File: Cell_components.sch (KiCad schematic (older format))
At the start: 12 parts, among them Q6 Q_NMOS_GSD

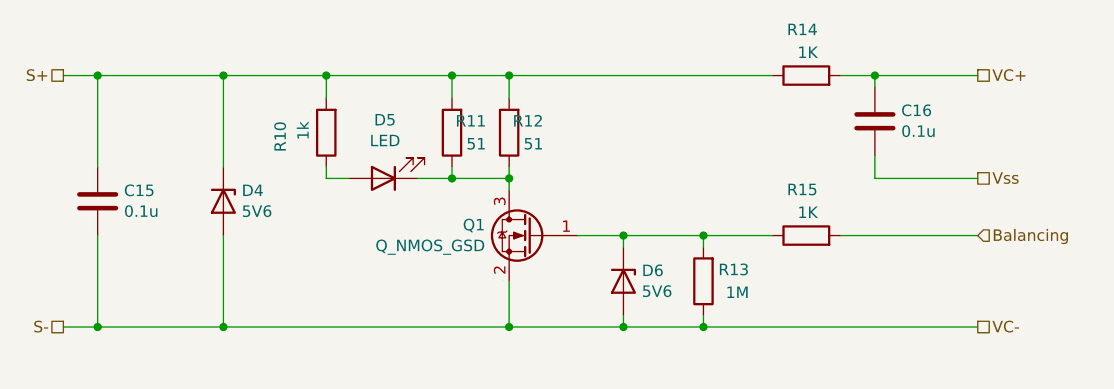
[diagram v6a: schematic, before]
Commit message: Add files via upload
Placed additional via's to BQ76-IC and removed soldermask beneath (to allow for soldering of thermal pad without hot air). Generated GERBER-, BOM- (for SMD parts) and POS-file.
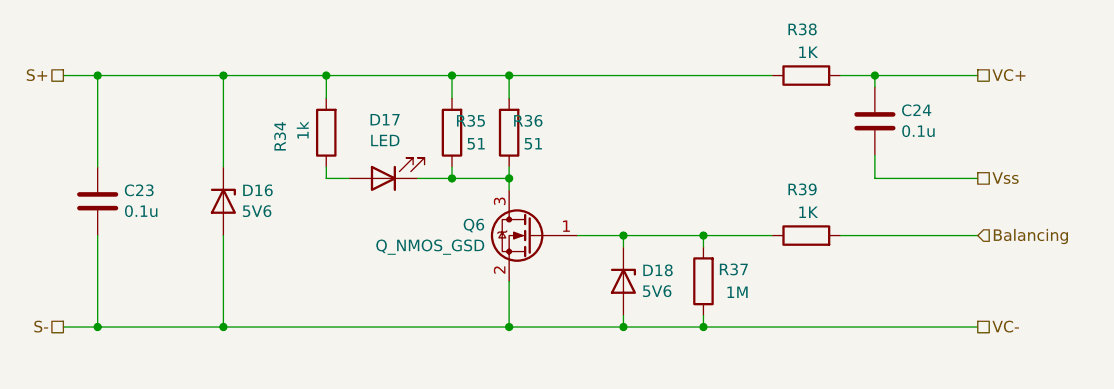
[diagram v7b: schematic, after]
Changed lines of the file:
@@
 $Descr User 7874 5906
 encoding utf-8
-Sheet 3 7
+Sheet 7 7
 Title ""
 Date ""
@@
 AR Path="/5FA9BBC5/5FB16918" Ref="C19"  Part="1"
 AR Path="/5FA9D4E1/5FB16918" Ref="C21"  Part="1"
-F 0 "C15" H 1965 2096 50  0000 L CNN
+F 0 "C23" H 1965 2096 50  0000 L CNN
 F 1 "0.1u " H 1965 2005 50  0000 L CNN
 F 2 "Capacitor_SMD:C_0805_2012Metric_Pad1.15x1.40mm_HandSolder" H 1888 1900 50  0001 C CNN
@@
 AR Path="/5FA9BBC5/5FB1FCF3" Ref="C20"  Part="1"
 AR Path="/5FA9D4E1/5FB1FCF3" Ref="C22"  Part="1"
-F 0 "C16" H 5365 1746 50  0000 L CNN
+F 0 "C24" H 5365 1746 50  0000 L CNN
 F 1 "0.1u " H 5365 1655 50  0000 L CNN
 F 2 "Capacitor_SMD:C_0805_2012Metric_Pad1.15x1.40mm_HandSolder" H 5288 1550 50  0001 C CNN
@@
 AR Path="/5FA9D4E1/5FB211C7" Ref="R32"  Part="1"
 AR Path="/5FAA7870/5FB211C7" Ref="R38"  Part="1"
-F 0 "R14" V 5150 1450 50  0000 L CNN
+F 0 "R38" V 5150 1450 50  0000 L CNN
 F 1 "1K" V 5050 1450 50  0000 L CNN
 F 2 "Resistor_SMD:R_0603_1608Metric_Pad1.05x0.95mm_HandSolder" V 4880 1500 50  0001 C CNN
@@
 AR Path="/5FA9D4E1/5FB24803" Ref="R33"  Part="1"
 AR Path="/5FAA7870/5FB24803" Ref="R39"  Part="1"
-F 0 "R15" V 5150 2150 50  0000 L CNN
+F 0 "R39" V 5150 2150 50  0000 L CNN
 F 1 "1K" V 5050 2150 50  0000 L CNN
 F 2 "Resistor_SMD:R_0603_1608Metric_Pad1.05x0.95mm_HandSolder" V 4880 2200 50  0001 C CNN
@@
 AR Path="/5FA9D4E1/5FB273BA" Ref="R31"  Part="1"
 AR Path="/5FAA7870/5FB273BA" Ref="R37"  Part="1"
-F 0 "R13" H 4300 2350 50  0000 L CNN
+F 0 "R37" H 4300 2350 50  0000 L CNN
 F 1 "1M" H 4300 2450 50  0000 L CNN
 F 2 "Resistor_SMD:R_0805_2012Metric_Pad1.15x1.40mm_HandSolder" V 4430 2400 50  0001 C CNN
@@
 AR Path="/5FA9BBC5/5FB35DA2" Ref="D12"  Part="1"
 AR Path="/5FA9D4E1/5FB35DA2" Ref="D15"  Part="1"
-F 0 "D6" V 4104 2480 50  0000 L CNN
+F 0 "D18" V 4104 2480 50  0000 L CNN
 F 1 "5V6" V 4195 2480 50  0000 L CNN
 F 2 "Diode_SMD:D_SOD-123" H 4150 2400 50  0001 C CNN
@@
 AR Path="/5FA9D4E1/5FAFC2A5" Ref="R30"  Part="1"
 AR Path="/5FAA7870/5FAFC2A5" Ref="R36"  Part="1"
-F 0 "R12" H 3500 1700 50  0000 L CNN
+F 0 "R36" H 3500 1700 50  0000 L CNN
 F 1 "51" H 3500 1800 50  0000 L CNN
 F 2 "Resistor_SMD:R_2512_6332Metric_Pad1.52x3.35mm_HandSolder" V 3580 1750 50  0001 C CNN
@@
 AR Path="/5FA9D4E1/5FAFE41B" Ref="R29"  Part="1"
 AR Path="/5FAA7870/5FAFE41B" Ref="R35"  Part="1"
-F 0 "R11" H 3250 1700 50  0000 L CNN
+F 0 "R35" H 3250 1700 50  0000 L CNN
 F 1 "51" H 3250 1800 50  0000 L CNN
 F 2 "Resistor_SMD:R_2512_6332Metric_Pad1.52x3.35mm_HandSolder" V 3330 1750 50  0001 C CNN
@@
 AR Path="/5FA9D4E1/5FB07EF1" Ref="R28"  Part="1"
 AR Path="/5FAA7870/5FB07EF1" Ref="R34"  Part="1"
-F 0 "R10" V 3050 1700 50  0000 L CNN
+F 0 "R34" V 3050 1700 50  0000 L CNN
 F 1 "1k" V 2950 1700 50  0000 L CNN
 F 2 "Resistor_SMD:R_0603_1608Metric_Pad1.05x0.95mm_HandSolder" V 2780 1750 50  0001 C CNN
@@
 AR Path="/5FA9D4E1/5FB0934F" Ref="D14"  Part="1"
 AR Path="/5FAA7870/5FB0934F" Ref="D17"  Part="1"
-F 0 "D5" H 3093 1695 50  0000 C CNN
+F 0 "D17" H 3093 1695 50  0000 C CNN
 F 1 "LED" H 3093 1786 50  0000 C CNN
 F 2 "LED_SMD:LED_0805_2012Metric_Pad1.15x1.40mm_HandSolder" H 3100 1950 50  0001 C CNN
@@
 AR Path="/5FA9BBC5/601F5F7C" Ref="Q4"  Part="1"
 AR Path="/5FA9D4E1/601F5F7C" Ref="Q5"  Part="1"
-F 0 "Q1" H 3955 2246 50  0000 L CNN
+F 0 "Q6" H 3955 2246 50  0000 L CNN
 F 1 "Q_NMOS_GSD" H 3955 2155 50  0000 L CNN
 F 2 "Package_TO_SOT_SMD:SOT-23" H 3950 2300 50  0001 C CNN
@@
 AR Path="/5FA9BBC5/5FB3410E" Ref="D10"  Part="1"
 AR Path="/5FA9D4E1/5FB3410E" Ref="D13"  Part="1"
-F 0 "D4" V 2354 2130 50  0000 L CNN
+F 0 "D16" V 2354 2130 50  0000 L CNN
 F 1 "5V6" V 2445 2130 50  0000 L CNN
 F 2 "Diode_SMD:D_SOD-123" H 2400 2050 50  0001 C CNN
